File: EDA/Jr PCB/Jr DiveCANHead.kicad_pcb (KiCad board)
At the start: 2 copper layers, 63 x 32 mm, 63 parts, among them J2 Conn_01x05_Pin, J3 Conn_ARM_SWD_TagConnect_TC203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, J4 Conn_01x05_Pin, Q1 SI2302, SW1 RST, SW2 RST, U1 STM32L431RCTx, U2 TCAN334, U3 TPS2121, U4 TPS7A2533DRVR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

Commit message: Jr 1.1 board revision
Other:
- board text added: "DIVE CAN CONTROLLER JR 1.1"
- board text removed: "DIVE CAN CONTROLLER JR 1.0"

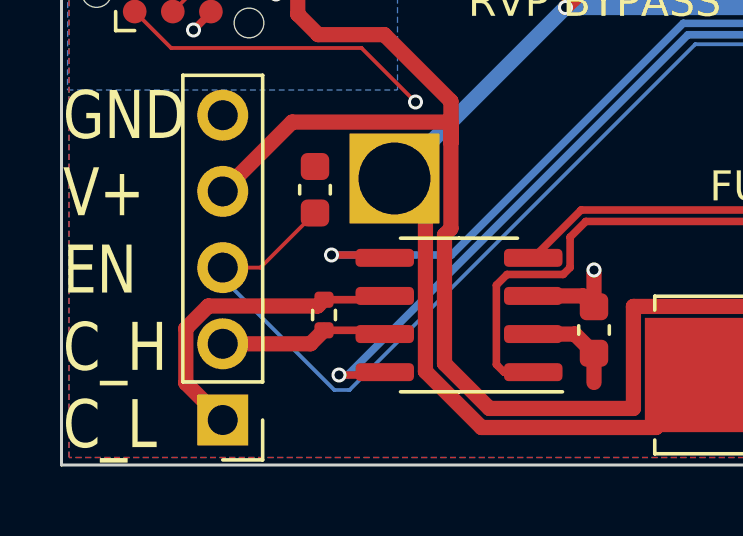
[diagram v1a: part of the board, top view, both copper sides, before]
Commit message: switch R35 to JLC basic on Main and Jr boards
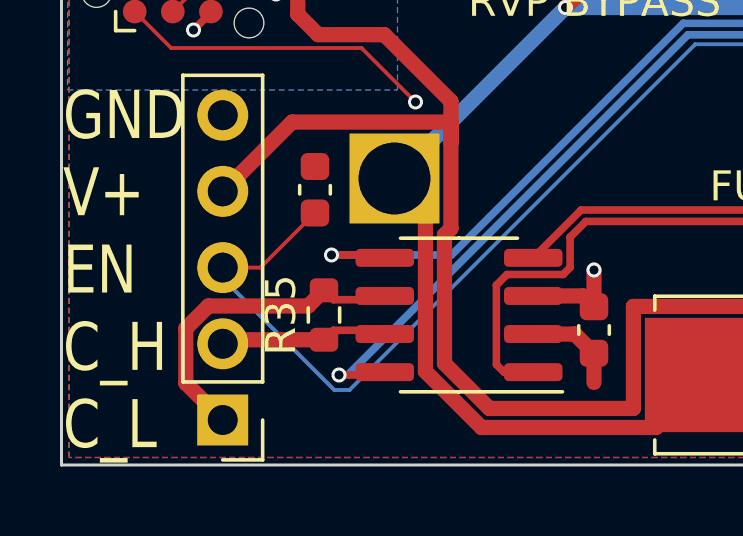
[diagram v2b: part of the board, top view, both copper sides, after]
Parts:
- R35: footprint Resistor_SMD:R_0402_1005Metric -> Resistor_SMD:R_0603_1608Metric
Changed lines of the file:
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@@
 		)
 	)
-	(footprint "Resistor_SMD:R_0402_1005Metric"
+	(footprint "Resistor_SMD:R_0603_1608Metric"
 		(layer "F.Cu")
 		(at 79.75 98.5 90)
-		(descr "Resistor SMD 0402 (1005 Metric), square (rectangular) end terminal, IPC_7351 nominal, (Body size source: IPC-SM-782 page 72, https://www.pcb-3d.com/wordpress/wp-content/uploads/ipc-sm-782a_amendment_1_and_2.pdf), generated with kicad-footprint-generator")
+		(descr "Resistor SMD 0603 (1608 Metric), square (rectangular) end terminal, IPC-7351 nominal, (Body size source: IPC-SM-782 page 72, https://www.pcb-3d.com/wordpress/wp-content/uploads/ipc-sm-782a_amendment_1_and_2.pdf), generated with kicad-footprint-generator")
 		(tags "resistor")
 		(property "Reference" "R35"
-			(at 0 -2.25 180)
+			(at 0 -1.43 90)
 			(layer "F.SilkS")
-			(hide yes)
 			(effects
 				(font
@@
 		)
 		(property "Value" "560"
-			(at 0 1.17 90)
+			(at 0 1.43 90)
 			(layer "F.Fab")
 			(effects
@@
 		(property "Datasheet" "~"
 			(at 0 0 90)
-			(unlocked yes)
 			(layer "F.Fab")
 			(hide yes)
@@
 		(property "Description" ""
 			(at 0 0 90)
-			(unlocked yes)
 			(layer "F.Fab")
 			(hide yes)
@@
 			)
 		)
-		(property "MPN" "C163460"
-			(at 0 0 0)
+		(property "MPN" "C23204"
+			(at 0 0 90)
+			(unlocked yes)
 			(layer "F.Fab")
 			(hide yes)
@@
 		(attr smd)
 		(fp_line
-			(start -0.153641 -0.38)
-			(end 0.153641 -0.38)
+			(start -0.237258 -0.5225)
+			(end 0.237258 -0.5225)
 			(stroke
 				(width 0.12)
@@
 		)
 		(fp_line
-			(start -0.153641 0.38)
-			(end 0.153641 0.38)
+			(start -0.237258 0.5225)
+			(end 0.237258 0.5225)
 			(stroke
 				(width 0.12)
@@
 			(layer "F.SilkS")
 		)
-		(fp_line
-			(start 0.93 -0.47)
-			(end 0.93 0.47)
-			(stroke
-				(width 0.05)
-				(type solid)
-			)
-			(layer "F.CrtYd")
-		)
-		(fp_line
-			(start -0.93 -0.47)
-			(end 0.93 -0.47)
-			(stroke
-				(width 0.05)
-				(type solid)
-			)
-			(layer "F.CrtYd")
-		)
-		(fp_line
-			(start 0.93 0.47)
-			(end -0.93 0.47)
-			(stroke
-				(width 0.05)
-				(type solid)
-			)
-			(layer "F.CrtYd")
-		)
-		(fp_line
-			(start -0.93 0.47)
-			(end -0.93 -0.47)
+		(fp_rect
+			(start -1.48 -0.73)
+			(end 1.48 0.73)
 			(stroke
 				(width 0.05)
 				(type solid)
 			)
+			(fill no)
 			(layer "F.CrtYd")
 		)
-		(fp_line
-			(start 0.525 -0.27)
-			(end 0.525 0.27)
-			(stroke
-				(width 0.1)
-				(type solid)
-			)
-			(layer "F.Fab")
-		)
-		(fp_line
-			(start -0.525 -0.27)
-			(end 0.525 -0.27)
-			(stroke
-				(width 0.1)
-				(type solid)
-			)
-			(layer "F.Fab")
-		)
-		(fp_line
-			(start 0.525 0.27)
-			(end -0.525 0.27)
-			(stroke
-				(width 0.1)
-				(type solid)
-			)
-			(layer "F.Fab")
-		)
-		(fp_line
-			(start -0.525 0.27)
-			(end -0.525 -0.27)
+		(fp_rect
+			(start -0.8 -0.4125)
+			(end 0.8 0.4125)
 			(stroke
 				(width 0.1)
 				(type solid)
 			)
+			(fill no)
 			(layer "F.Fab")
 		)
@@
 			(effects
 				(font
-					(size 0.26 0.26)
-					(thickness 0.04)
+					(size 0.4 0.4)
+					(thickness 0.06)
 				)
 			)
 		)
 		(pad "1" smd roundrect
-			(at -0.51 0 90)
-			(size 0.54 0.64)
+			(at -0.825 0 90)
+			(size 0.8 0.95)
 			(layers "F.Cu" "F.Mask" "F.Paste")
 			(roundrect_rratio 0.25)
@@
 		)
 		(pad "2" smd roundrect
-			(at 0.51 0 90)
-			(size 0.54 0.64)
+			(at 0.825 0 90)
+			(size 0.8 0.95)
 			(layers "F.Cu" "F.Mask" "F.Paste")
 			(roundrect_rratio 0.25)
@@
 		)
 		(embedded_fonts no)
-		(model "${KICAD6_3DMODEL_DIR}/Resistor_SMD.3dshapes/R_0402_1005Metric.wrl"
+		(model "${KICAD9_3DMODEL_DIR}/Resistor_SMD.3dshapes/R_0603_1608Metric.step"
 			(offset
 				(xyz 0 0 0)
@@
 	)
 	(segment
-		(start 79.75 99.01)
+		(start 80.065 99.01)
 		(end 81.65 99.01)
 		(width 0.254)
@@
 	)
 	(segment
-		(start 79.3 99.46)
-		(end 79.75 99.01)
+		(start 79.75 99.325)
+		(end 76.51 99.325)
 		(width 0.508)
 		(layer "F.Cu")
@@
 	)
 	(segment
-		(start 76.375 99.46)
-		(end 79.3 99.46)
-		(width 0.508)
+		(start 79.75 99.325)
+		(end 80.065 99.01)
+		(width 0.254)
 		(layer "F.Cu")
 		(net 18)
 	)
 	(segment
-		(start 79.54 98.2)
-		(end 79.75 97.99)
+		(start 76.51 99.325)
+		(end 76.375 99.46)
 		(width 0.508)
 		(layer "F.Cu")
-		(net 19)
+		(net 18)
 	)
 	(segment
-		(start 75.894103 98.2)
-		(end 79.54 98.2)
+		(start 75.144 100.769)
+		(end 75.144 98.950103)
 		(width 0.508)
 		(layer "F.Cu")
@@
 	)
 	(segment
-		(start 79.75 97.99)
-		(end 81.65 97.99)
-		(width 0.254)
+		(start 79.225 98.2)
+		(end 79.75 97.675)
+		(width 0.508)
 		(layer "F.Cu")
 		(net 19)
 	)
 	(segment
-		(start 75.144 100.769)
-		(end 75.144 98.950103)
+		(start 75.144 98.950103)
+		(end 75.894103 98.2)
 		(width 0.508)
 		(layer "F.Cu")
@@
 	)
 	(segment
-		(start 75.144 98.950103)
-		(end 75.894103 98.2)
+		(start 79.75 97.675)
+		(end 80.065 97.99)
+		(width 0.254)
+		(layer "F.Cu")
+		(net 19)
+	)
+	(segment
+		(start 75.894103 98.2)
+		(end 79.225 98.2)
 		(width 0.508)
 		(layer "F.Cu")
 		(net 19)
+	)
+	(segment
+		(start 80.065 97.99)
+		(end 81.65 97.99)
+		(width 0.254)
+		(layer "F.Cu")
+		(net 19)
